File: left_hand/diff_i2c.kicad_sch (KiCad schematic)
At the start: 12 parts, among them J7 Conn_01x08, J8 Conn_01x03, U3 PCA9615DP

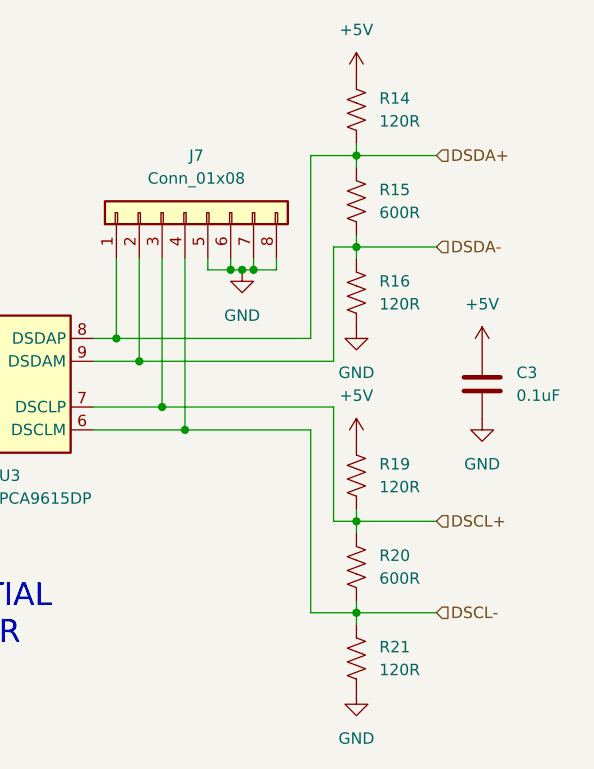
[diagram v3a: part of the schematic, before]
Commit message: Updated differential termination resistor values
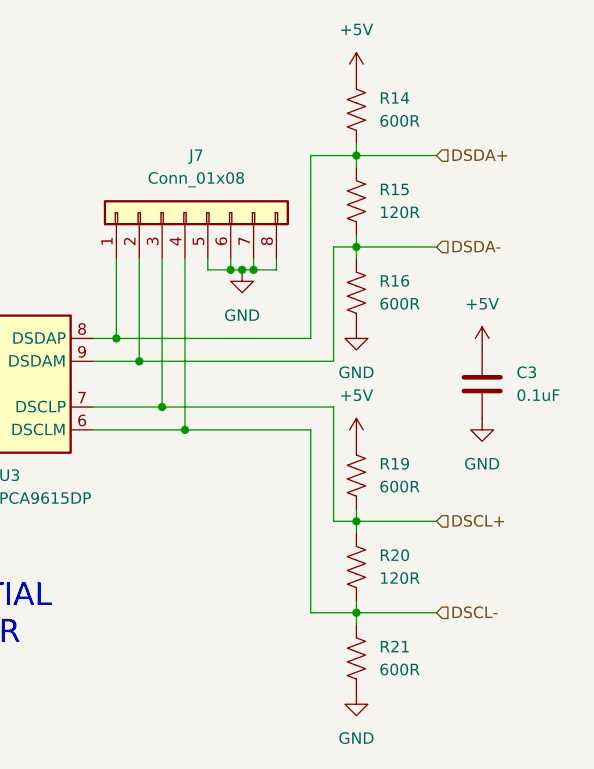
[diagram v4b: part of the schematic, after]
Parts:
- R14, R16, R19, R21: value 120R -> 600R
- R15, R20: value 600R -> 120R
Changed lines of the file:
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@@
 			)
 		)
-		(property "Value" "600R"
+		(property "Value" "120R"
 			(at 185.42 116.8399 0)
 			(effects
@@
 			)
 		)
-		(property "Value" "120R"
+		(property "Value" "600R"
 			(at 185.42 86.3599 0)
 			(effects
@@
 			)
 		)
-		(property "Value" "120R"
+		(property "Value" "600R"
 			(at 185.42 66.0399 0)
 			(effects
@@
 			)
 		)
-		(property "Value" "600R"
+		(property "Value" "120R"
 			(at 185.42 76.1999 0)
 			(effects
@@
 			)
 		)
-		(property "Value" "120R"
+		(property "Value" "600R"
 			(at 185.42 106.6799 0)
 			(effects
@@
 			)
 		)
-		(property "Value" "120R"
+		(property "Value" "600R"
 			(at 185.42 126.9999 0)
 			(effects

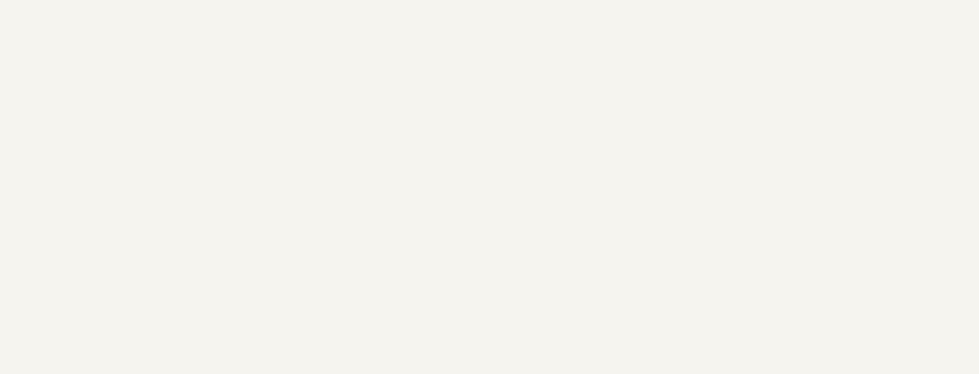
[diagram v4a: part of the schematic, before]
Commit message: Added drawing information boxes
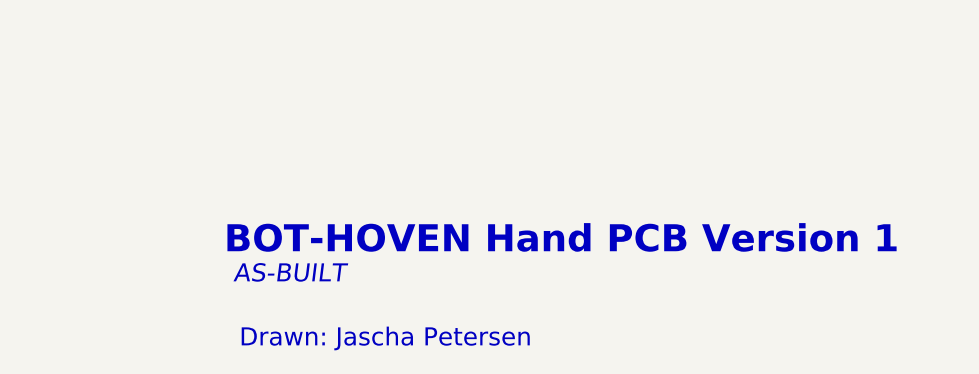
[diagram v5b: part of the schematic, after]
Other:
- note added: "AS-BUILT"
- note added: "BOT-HOVEN Hand PCB Version 1"
- note added: "Drawn: Jascha Petersen"
- title: (none) -> Hand PCB Differential I2C
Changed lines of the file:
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@@
 	(generator_version "8.0")
 	(paper "A4")
+	(title_block
+		(title "Hand PCB Differential I2C")
+	)
 	(junction
 		(at 139.7 83.82)
@@
 		)
 	)
+	(text "AS-BUILT"
+		(exclude_from_sim no)
+		(at 184.658 172.72 0)
+		(effects
+			(font
+				(size 2 2)
+				(italic yes)
+			)
+		)
+	)
+	(text "Drawn: Jascha Petersen"
+		(exclude_from_sim no)
+		(at 195.326 179.832 0)
+		(effects
+			(font
+				(size 2 2)
+			)
+		)
+	)
+	(text "BOT-HOVEN Hand PCB Version 1"
+		(exclude_from_sim no)
+		(at 214.884 168.91 0)
+		(effects
+			(font
+				(size 3 3)
+				(thickness 0.6)
+				(bold yes)
+			)
+		)
+	)
